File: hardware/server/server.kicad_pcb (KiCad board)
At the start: 2 copper layers, 41.9 x 50.8 mm, 12 parts

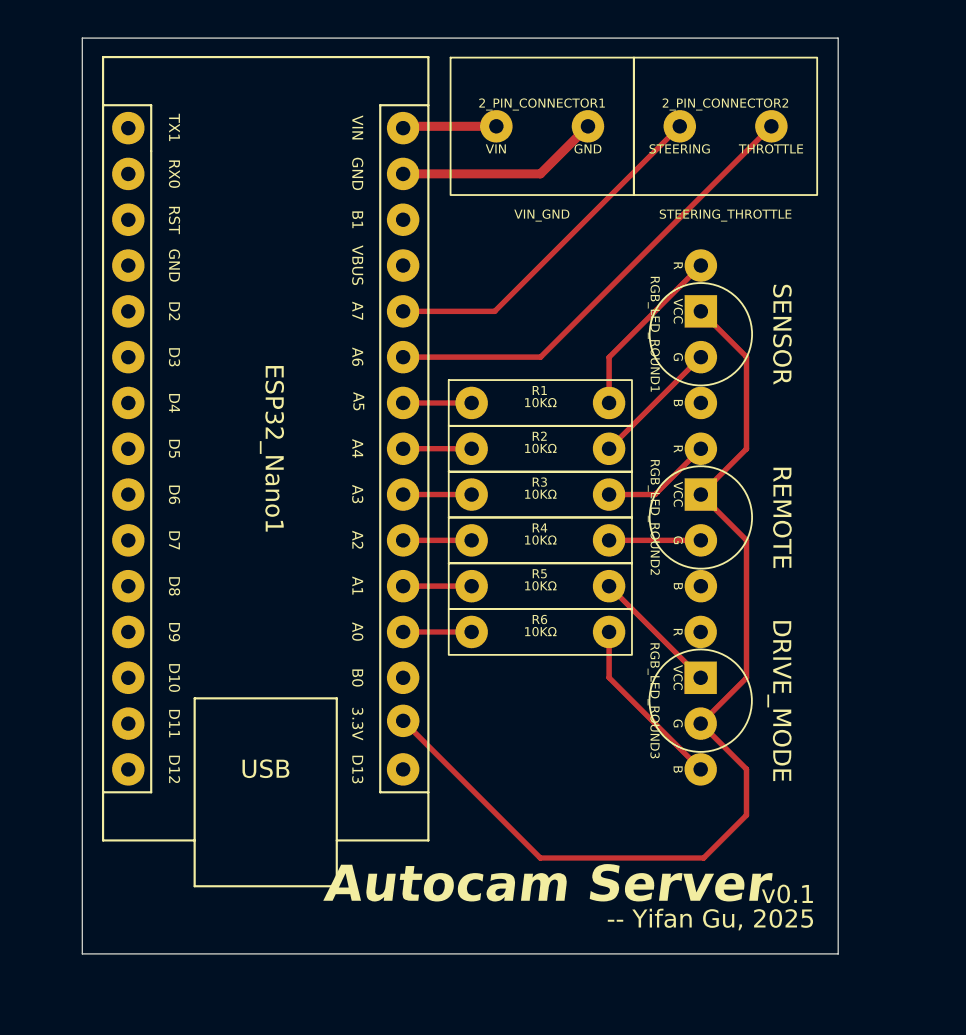
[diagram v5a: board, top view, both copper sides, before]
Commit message: hardware: Reroute the wires to fix unavailable PINs.
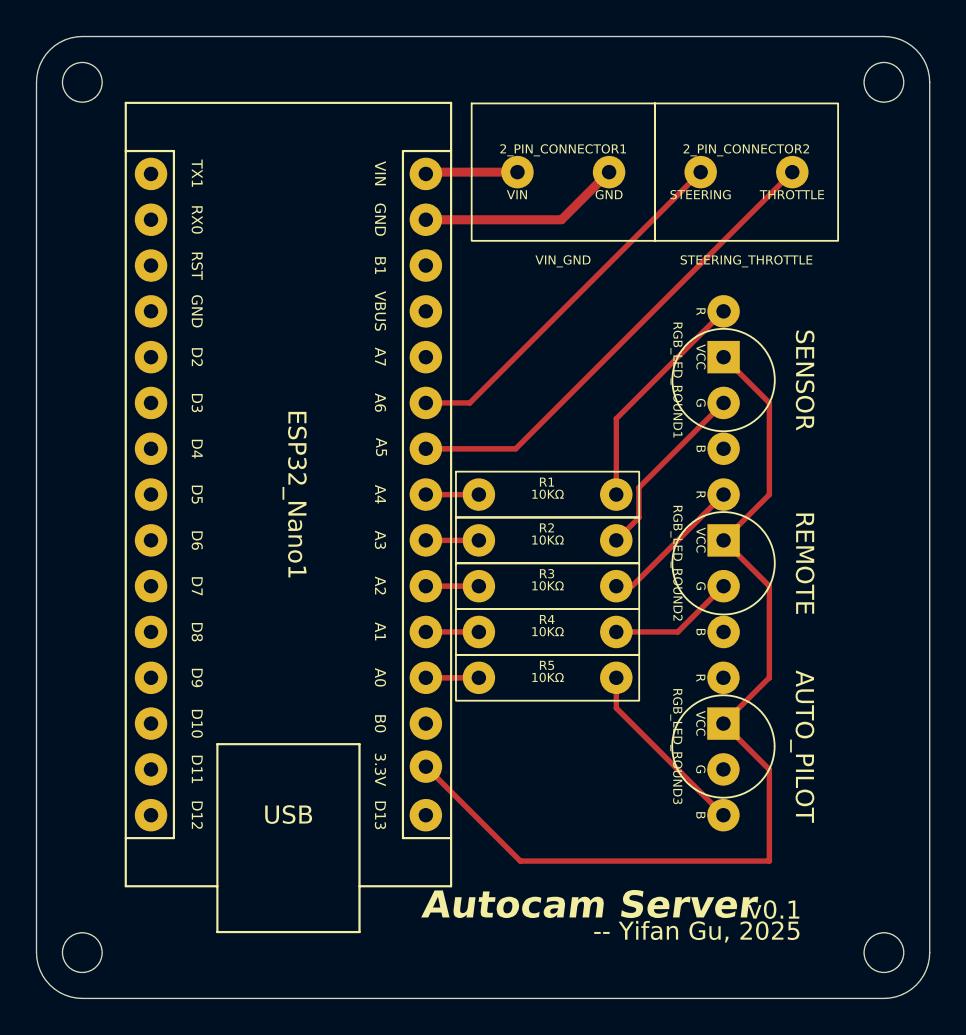
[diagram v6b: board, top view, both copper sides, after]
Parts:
- removed R6: 10KΩ, Autocam:Simple Resistor
- added REF**: MountingHole_2.2mm_M2, MountingHole:MountingHole_2.2mm_M2, F.Cu at (176.5, 71.1)
- added REF**: MountingHole_2.2mm_M2, MountingHole:MountingHole_2.2mm_M2, F.Cu at (132.1, 71.1)
- added REF**: MountingHole_2.2mm_M2, MountingHole:MountingHole_2.2mm_M2, F.Cu at (132.1, 119.4)
- added REF**: MountingHole_2.2mm_M2, MountingHole:MountingHole_2.2mm_M2, F.Cu at (176.5, 119.4)
- RGB_LED_ROUND3: value DRIVE_MODE -> AUTO_PILOT
- moved R1 5.10 mm to (154.1, 94.0)
- moved R2 5.10 mm to (154.1, 96.5)
- moved R3 5.10 mm to (154.1, 99.1)
- moved R4 5.10 mm to (154.1, 101.6)
- moved R5 5.10 mm to (154.1, 104.1)
- moved ESP32_Nano1 2.84 mm to (135.9, 76.2)
- moved RGB_LED_ROUND2 2.84 mm to (167.6, 97.8)
- moved RGB_LED_ROUND3 2.84 mm to (167.6, 108.0)
- moved RGB_LED_ROUND1 2.84 mm to (167.6, 87.6)
- moved 2_PIN_CONNECTOR1 2.80 mm to (153.7, 79.9)
- moved 2_PIN_CONNECTOR2 2.79 mm to (163.8, 79.9)
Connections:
- ESP32_Nano1 pad 24: Net-(ESP32_Nano1-A5) -> Net-(2_PIN_CONNECTOR2-Pin_2)
- ESP32_Nano1 pad 25: Net-(2_PIN_CONNECTOR2-Pin_2) -> Net-(2_PIN_CONNECTOR2-Pin_1)
- ESP32_Nano1 pad 26: Net-(2_PIN_CONNECTOR2-Pin_1) -> unconnected-(ESP32_Nano1-A7-Pad26)
- R1 pad 1: Net-(ESP32_Nano1-A5) -> Net-(ESP32_Nano1-A4)
- R2 pad 1: Net-(ESP32_Nano1-A4) -> Net-(ESP32_Nano1-A3)
- R3 pad 1: Net-(ESP32_Nano1-A3) -> Net-(ESP32_Nano1-A2)
- R4 pad 1: Net-(ESP32_Nano1-A2) -> Net-(ESP32_Nano1-A1)
- R5 pad 1: Net-(ESP32_Nano1-A1) -> Net-(ESP32_Nano1-A0)
- R5 pad 2: Net-(RGB_LED_ROUND3-R) -> Net-(RGB_LED_ROUND3-B)
- RGB_LED_ROUND3 pad 1: Net-(RGB_LED_ROUND3-R) -> unconnected-(RGB_LED_ROUND3-R-Pad1)
- RGB_LED_ROUND3 pad 3: Net-(RGB_LED_ROUND3-G) -> unconnected-(RGB_LED_ROUND3-G-Pad3)
- RGB_LED_ROUND3 pad 4: unconnected-(RGB_LED_ROUND3-B-Pad4) -> Net-(RGB_LED_ROUND3-B)
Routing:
- net Net-(RGB_LED_ROUND3-B): track 0.00 -> 10.1 mm
- net Net-(RGB_LED_ROUND3-G): track 9.73 -> 0.00 mm
- net Net-(RGB_LED_ROUND3-R): track 7.19 -> 0.00 mm
- net Net-(ESP32_Nano1-A5): track 3.80 -> 0.00 mm
- net Net-(RGB_LED_ROUND1-G): track 7.19 -> 10.1 mm
- net Net-(RGB_LED_ROUND1-R): track 9.73 -> 12.6 mm
- net Net-(ESP32_Nano1-3.3V): track 56.4 -> 54.4 mm
- net Net-(RGB_LED_ROUND2-R): track 6.14 -> 8.06 mm
- net Net-(RGB_LED_ROUND2-G): track 5.09 -> 7.00 mm
- net Net-(2_PIN_CONNECTOR2-Pin_1): track 19.6 -> 20.5 mm
- net Net-(2_PIN_CONNECTOR2-Pin_2): track 25.7 -> 26.7 mm
- net Net-(ESP32_Nano1-A4): track 3.80 -> 2.94 mm
- net Net-(ESP32_Nano1-A3): track 3.80 -> 2.94 mm
- net Net-(ESP32_Nano1-A2): track 3.80 -> 2.94 mm
- net Net-(ESP32_Nano1-A1): track 3.80 -> 2.94 mm
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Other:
- board size 41.9 x 50.8 mm -> 49.5 x 53.3 mm

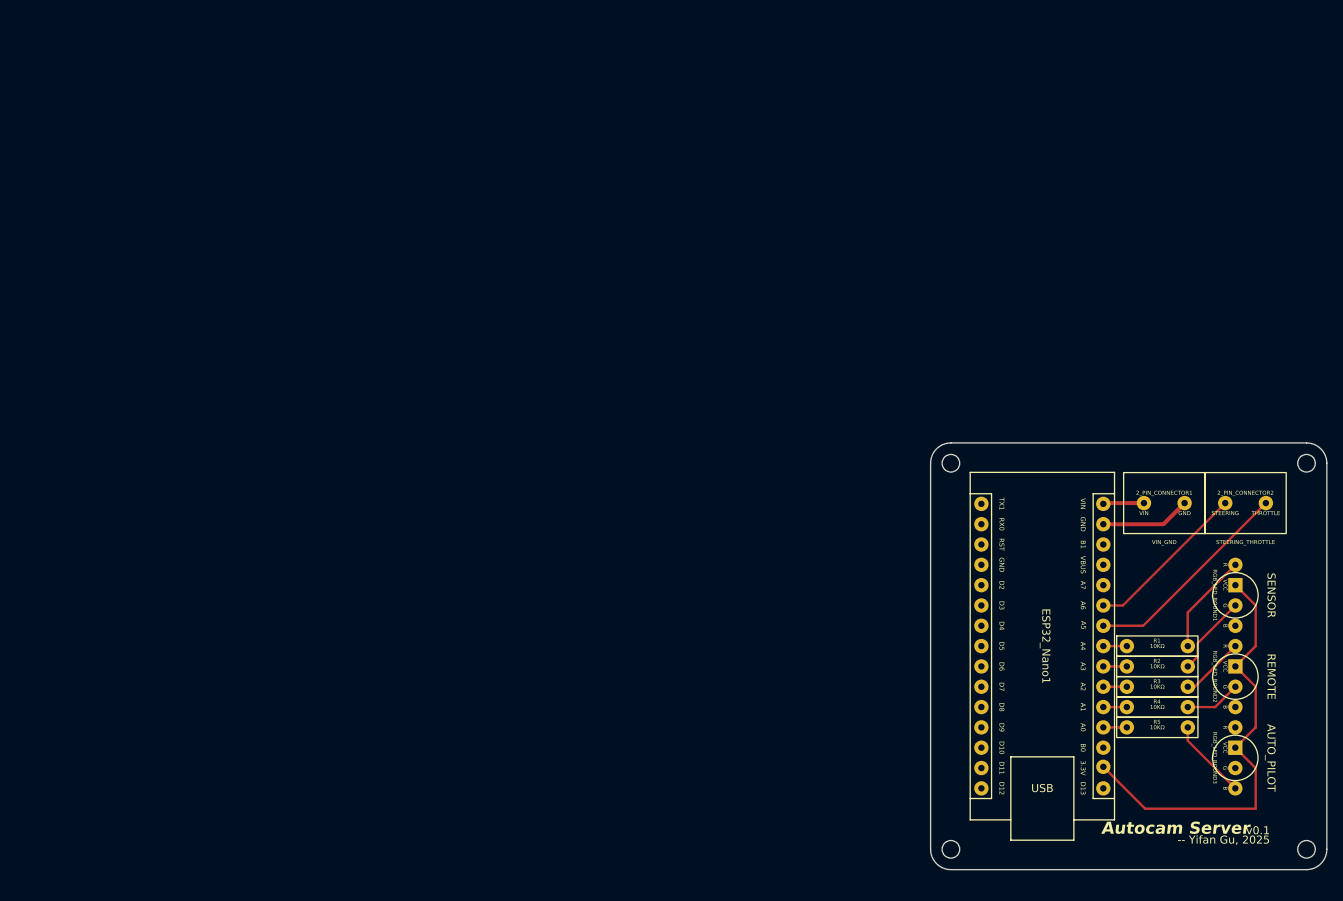
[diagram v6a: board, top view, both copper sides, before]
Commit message: hardware: Move the PCB to near the coordinate origin.
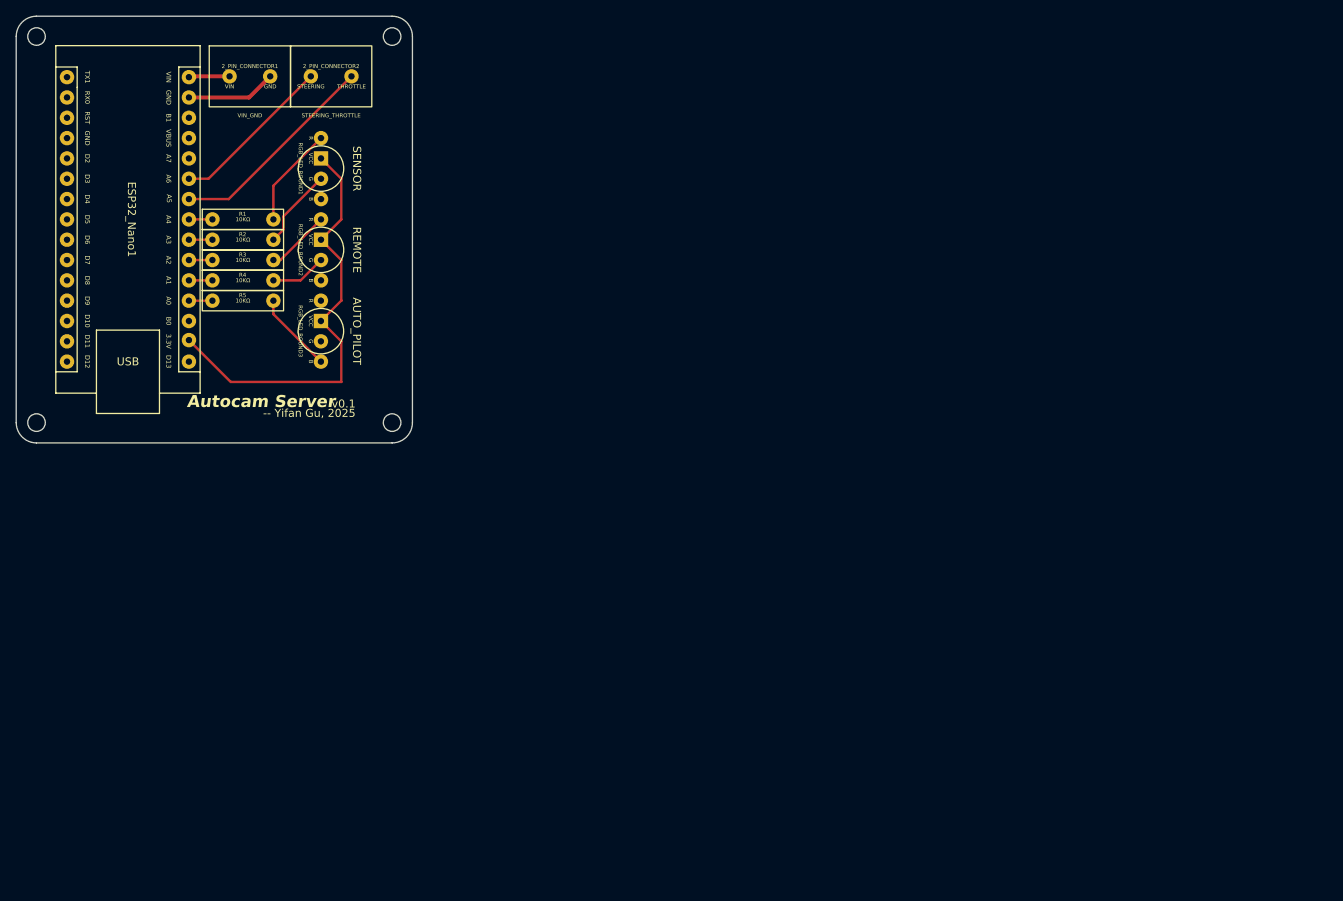
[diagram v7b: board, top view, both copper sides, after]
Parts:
- moved REF** 126.1 mm to (62.2, 17.8)
- moved REF** 126.1 mm to (17.8, 17.8)
- moved RGB_LED_ROUND3 126.1 mm to (53.3, 54.6)
- moved 2_PIN_CONNECTOR1 126.1 mm to (39.4, 26.6)
- moved 2_PIN_CONNECTOR2 126.1 mm to (49.5, 26.6)
- moved ESP32_Nano1 126.1 mm to (21.6, 22.9)
- moved R1 126.1 mm to (39.8, 40.6)
- moved R2 126.1 mm to (39.8, 43.2)
- moved R3 126.1 mm to (39.8, 45.7)
- moved R4 126.1 mm to (39.8, 48.3)
- moved R5 126.1 mm to (39.8, 50.8)
- moved REF** 126.1 mm to (17.8, 66.0)
- moved REF** 126.1 mm to (62.2, 66.0)
- moved RGB_LED_ROUND1 126.1 mm to (53.3, 34.3)
- moved RGB_LED_ROUND2 126.1 mm to (53.3, 44.5)
